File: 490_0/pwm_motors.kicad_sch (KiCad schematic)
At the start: 38 parts, among them J11 S2B-XH-A, J12 S2B-XH-A, J6 S2B-XH-A, J7 S2B-XH-A, J8 S2B-XH-A, Q1 NMOS, Q2 NMOS, Q3 NMOS, Q4 NMOS, Q5 NMOS, U6 PCA9685

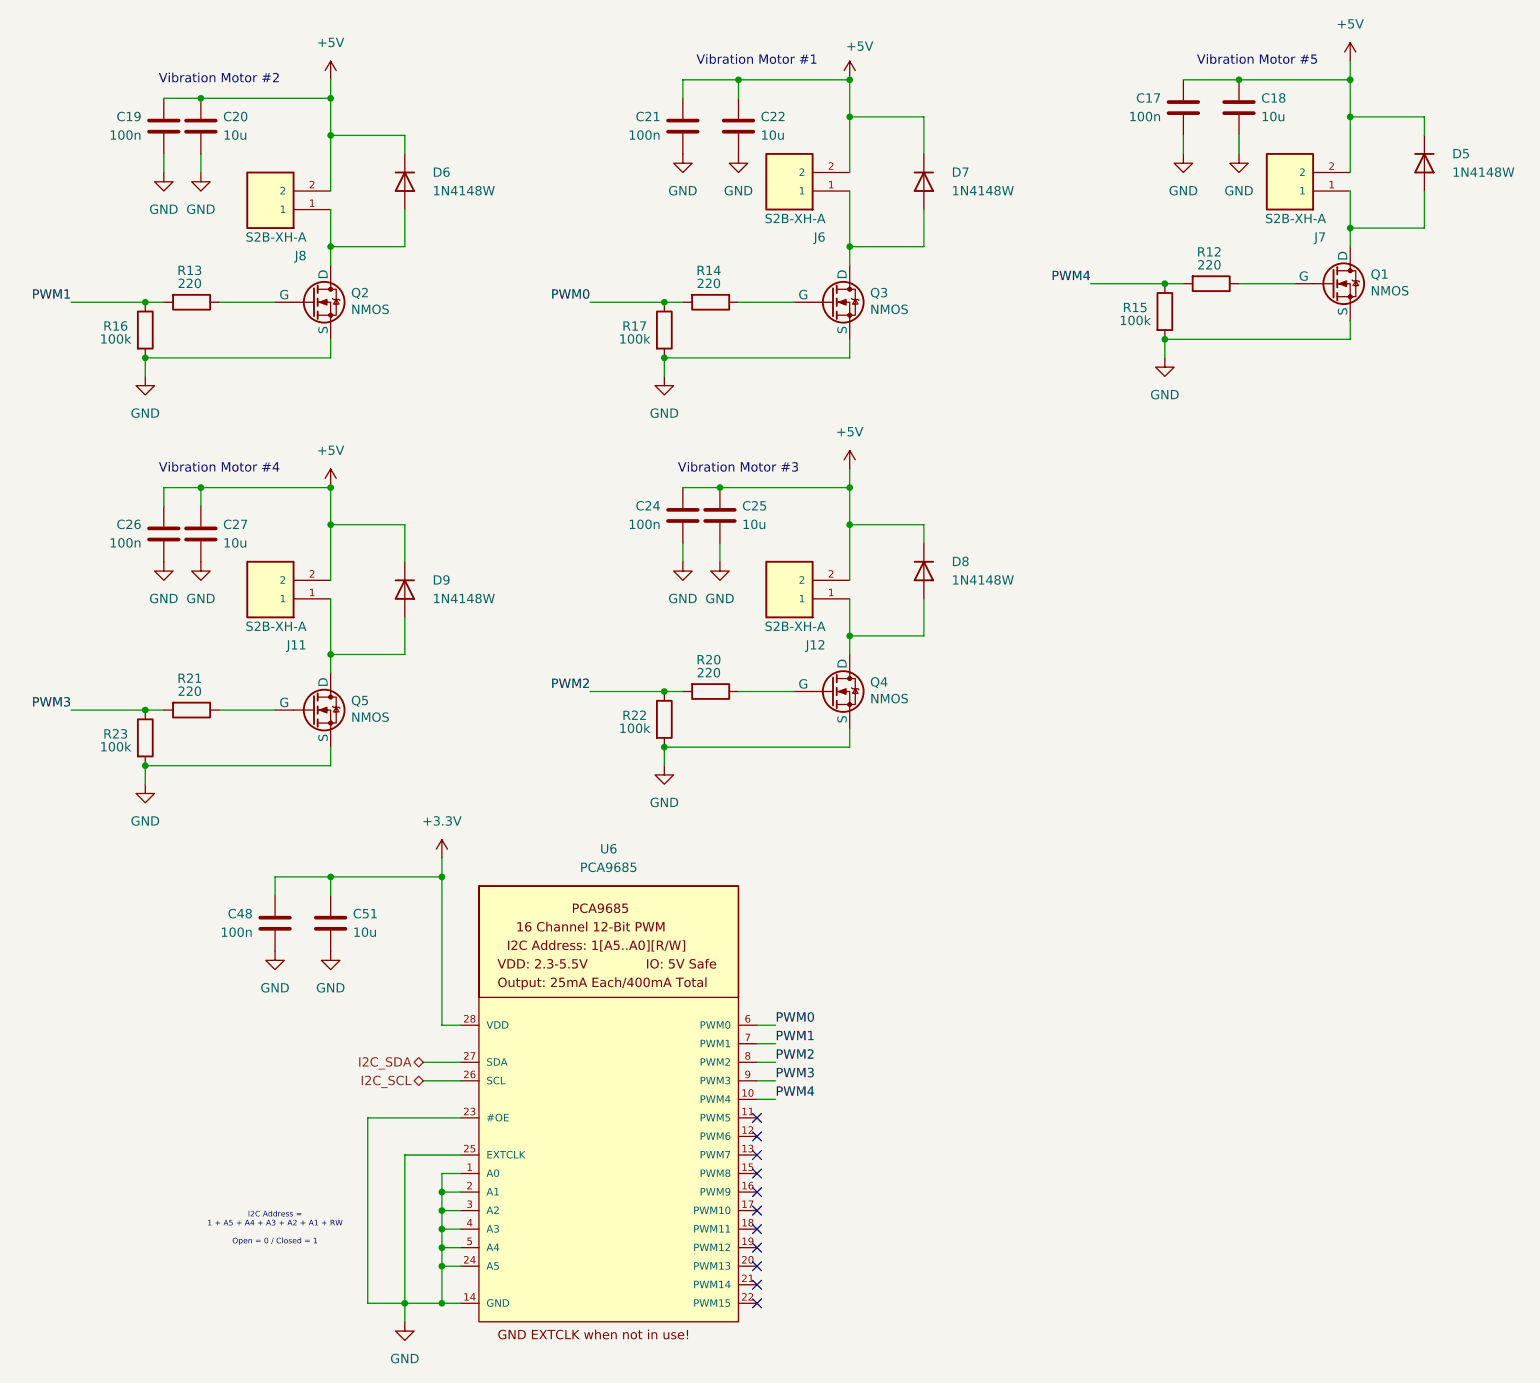
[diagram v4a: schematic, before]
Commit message: Implemented Dmitry comments
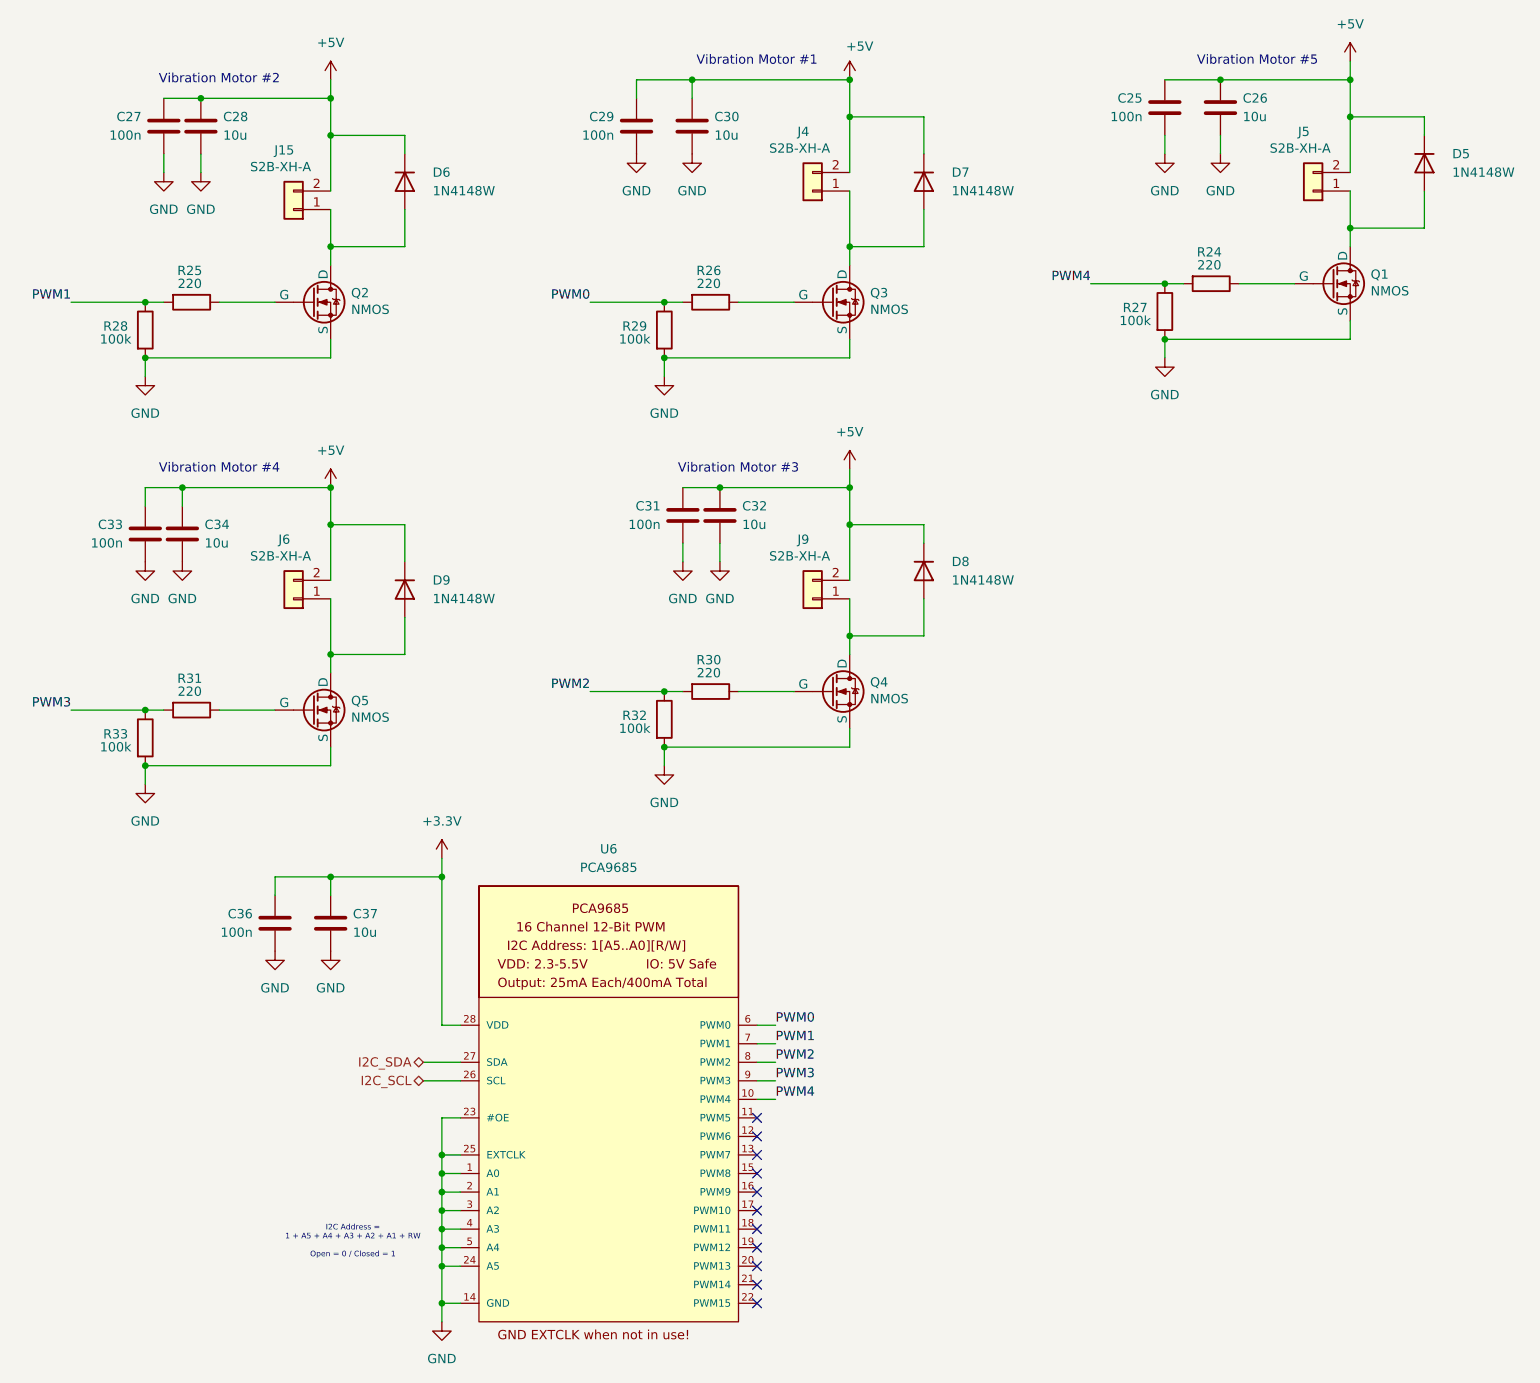
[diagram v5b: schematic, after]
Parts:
- removed J11, J12: S2B-XH-A, 4ms_Connector:Pins_1x08_2.54mm_TH, symbol capstone_parts:S2B-XH-A
- removed J6, J7, J8: S2B-XH-A, S2B-XH-A:JST_S2B-XH-A, symbol capstone_parts:S2B-XH-A
- added J15, J4, J5, J6, J9: S2B-XH-A, S2B-XH-A:JST_S2B-XH-A, symbol PCM_4ms_Connector:Conn_01x02
- renumbered C17 to C25, C18 to C26, C19 to C27, C20 to C28, C21 to C29, C22 to C30, C24 to C31, C25 to C32, C26 to C33, C27 to C34, C48 to C36, C51 to C37, R12 to R24, R13 to R25, R14 to R26, R15 to R27, R16 to R28, R17 to R29, R20 to R30, R21 to R31, R22 to R32, R23 to R33
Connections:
- net +5V: now also J15.2 (Pin_2), J4.2 (Pin_2), J5.2 (Pin_2), J6.2 (Pin_2), J9.2 (Pin_2)
- net at D8.2 (A), Q4.1 (D): now also J9.1 (Pin_1)
- net at D5.2 (A), Q1.1 (D): now also J5.1 (Pin_1)
- net at D6.2 (A), Q2.1 (D): now also J15.1 (Pin_1)
- net at D9.2 (A), Q5.1 (D): now also J6.1 (Pin_1)
- net at D7.2 (A), Q3.1 (D): now also J4.1 (Pin_1)
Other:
- moved on the sheet: C25, C26, C29, C30, C33, C34

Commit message: Final Fixes
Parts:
- J10: renamed from J9; now not fitted; now left out of the parts list
- J4, J5: now not fitted; now left out of the parts list
- J6: renamed from J15; now not fitted; now left out of the parts list
- J9: renamed from J6; now not fitted; now left out of the parts list
- renumbered C25 to C19, C26 to C20, C27 to C21, C28 to C22, C29 to C23, C30 to C24, C31 to C25, C32 to C26, C33 to C27, C34 to C28, C36 to C30, C37 to C31, R24 to R12, R25 to R13, R26 to R14, R27 to R15, R28 to R16, R29 to R17, R30 to R18, R31 to R19, R32 to R20, R33 to R21

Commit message: Implemented Dmitry recommendations
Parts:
- J10, J4, J5, J6, J9: now fitted
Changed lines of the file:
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@@
 		(in_bom no)
 		(on_board yes)
-		(dnp yes)
+		(dnp no)
 		(property "Reference" "J5"
 			(at 201.93 29.972 0)
@@
 		(in_bom no)
 		(on_board yes)
-		(dnp yes)
+		(dnp no)
 		(property "Reference" "J9"
 			(at 62.23 85.852 0)
@@
 		(in_bom no)
 		(on_board yes)
-		(dnp yes)
+		(dnp no)
 		(property "Reference" "J4"
 			(at 133.35 29.972 0)
@@
 		(in_bom no)
 		(on_board yes)
-		(dnp yes)
+		(dnp no)
 		(property "Reference" "J10"
 			(at 133.35 85.852 0)
@@
 		(in_bom no)
 		(on_board yes)
-		(dnp yes)
+		(dnp no)
 		(property "Reference" "J6"
 			(at 62.23 32.512 0)

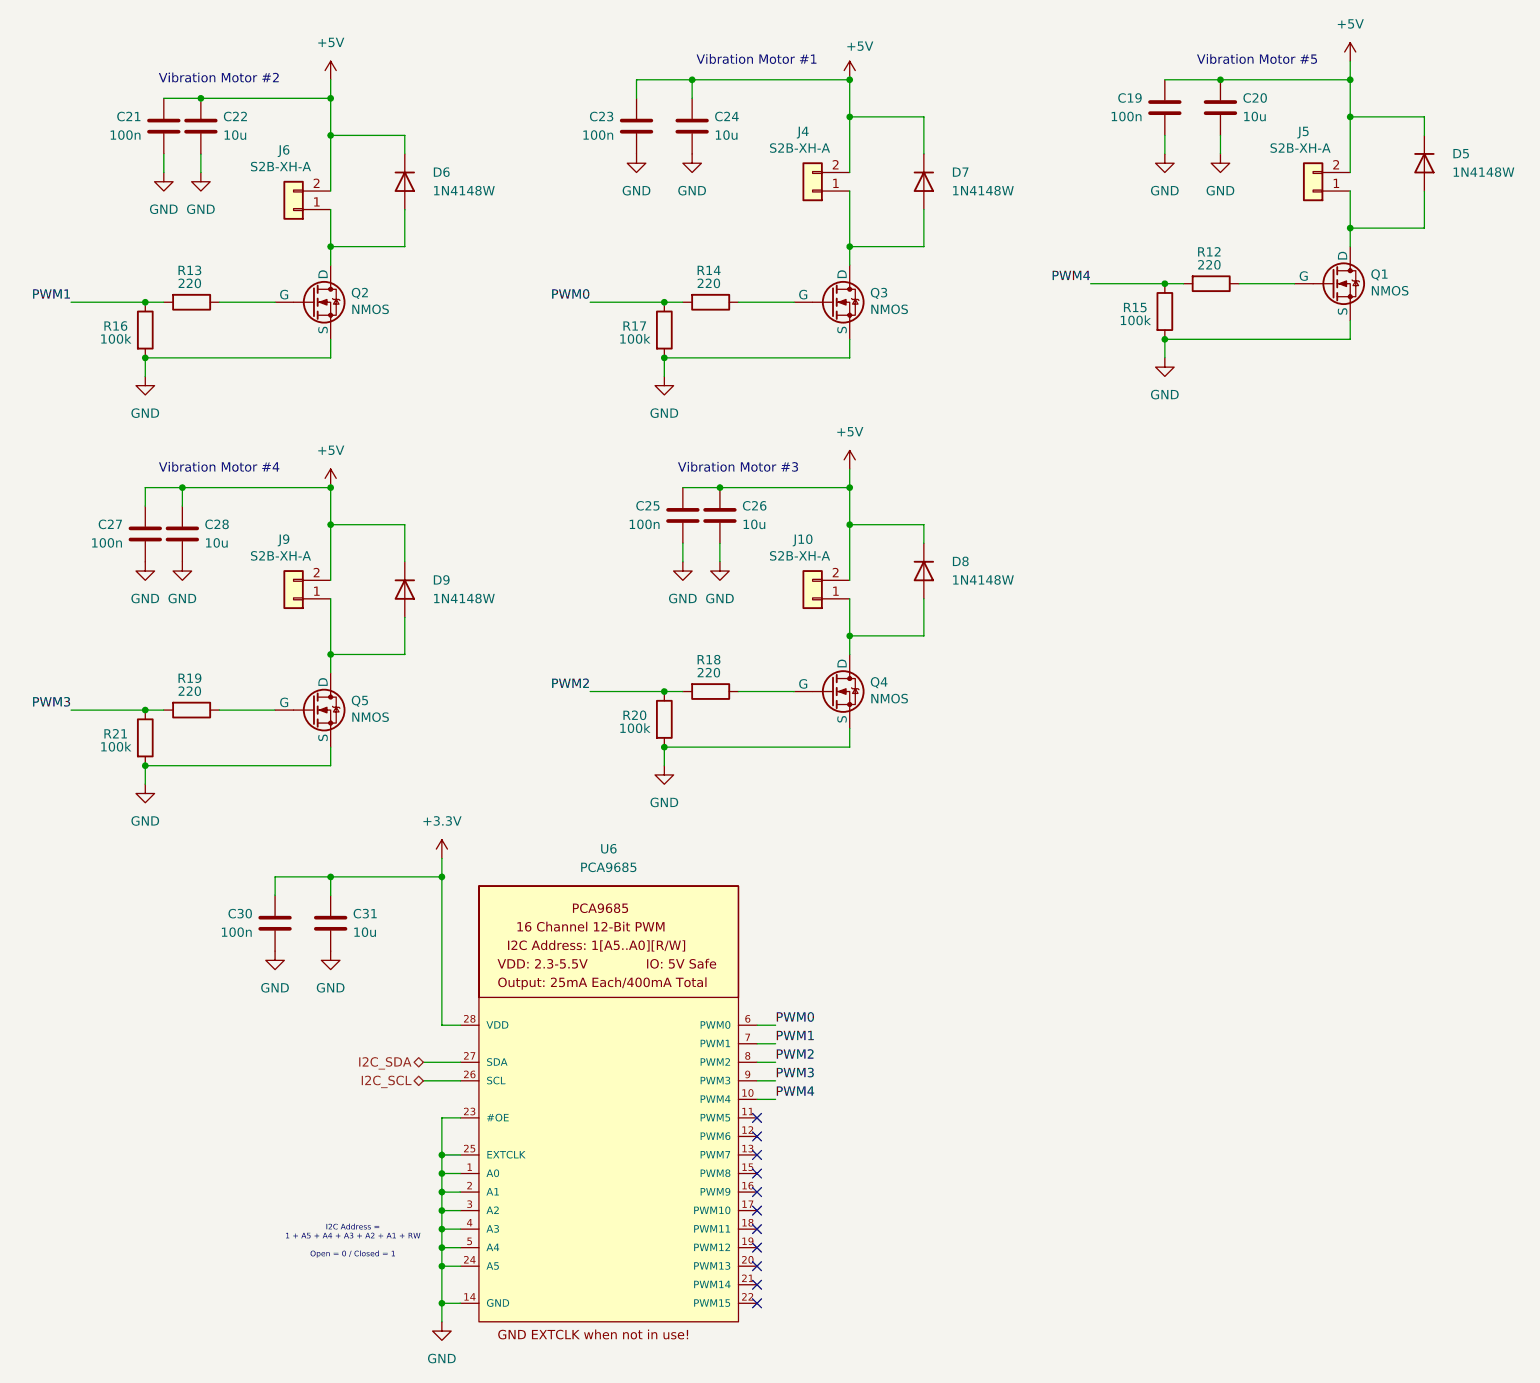
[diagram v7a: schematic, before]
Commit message: FFC to HDMI change
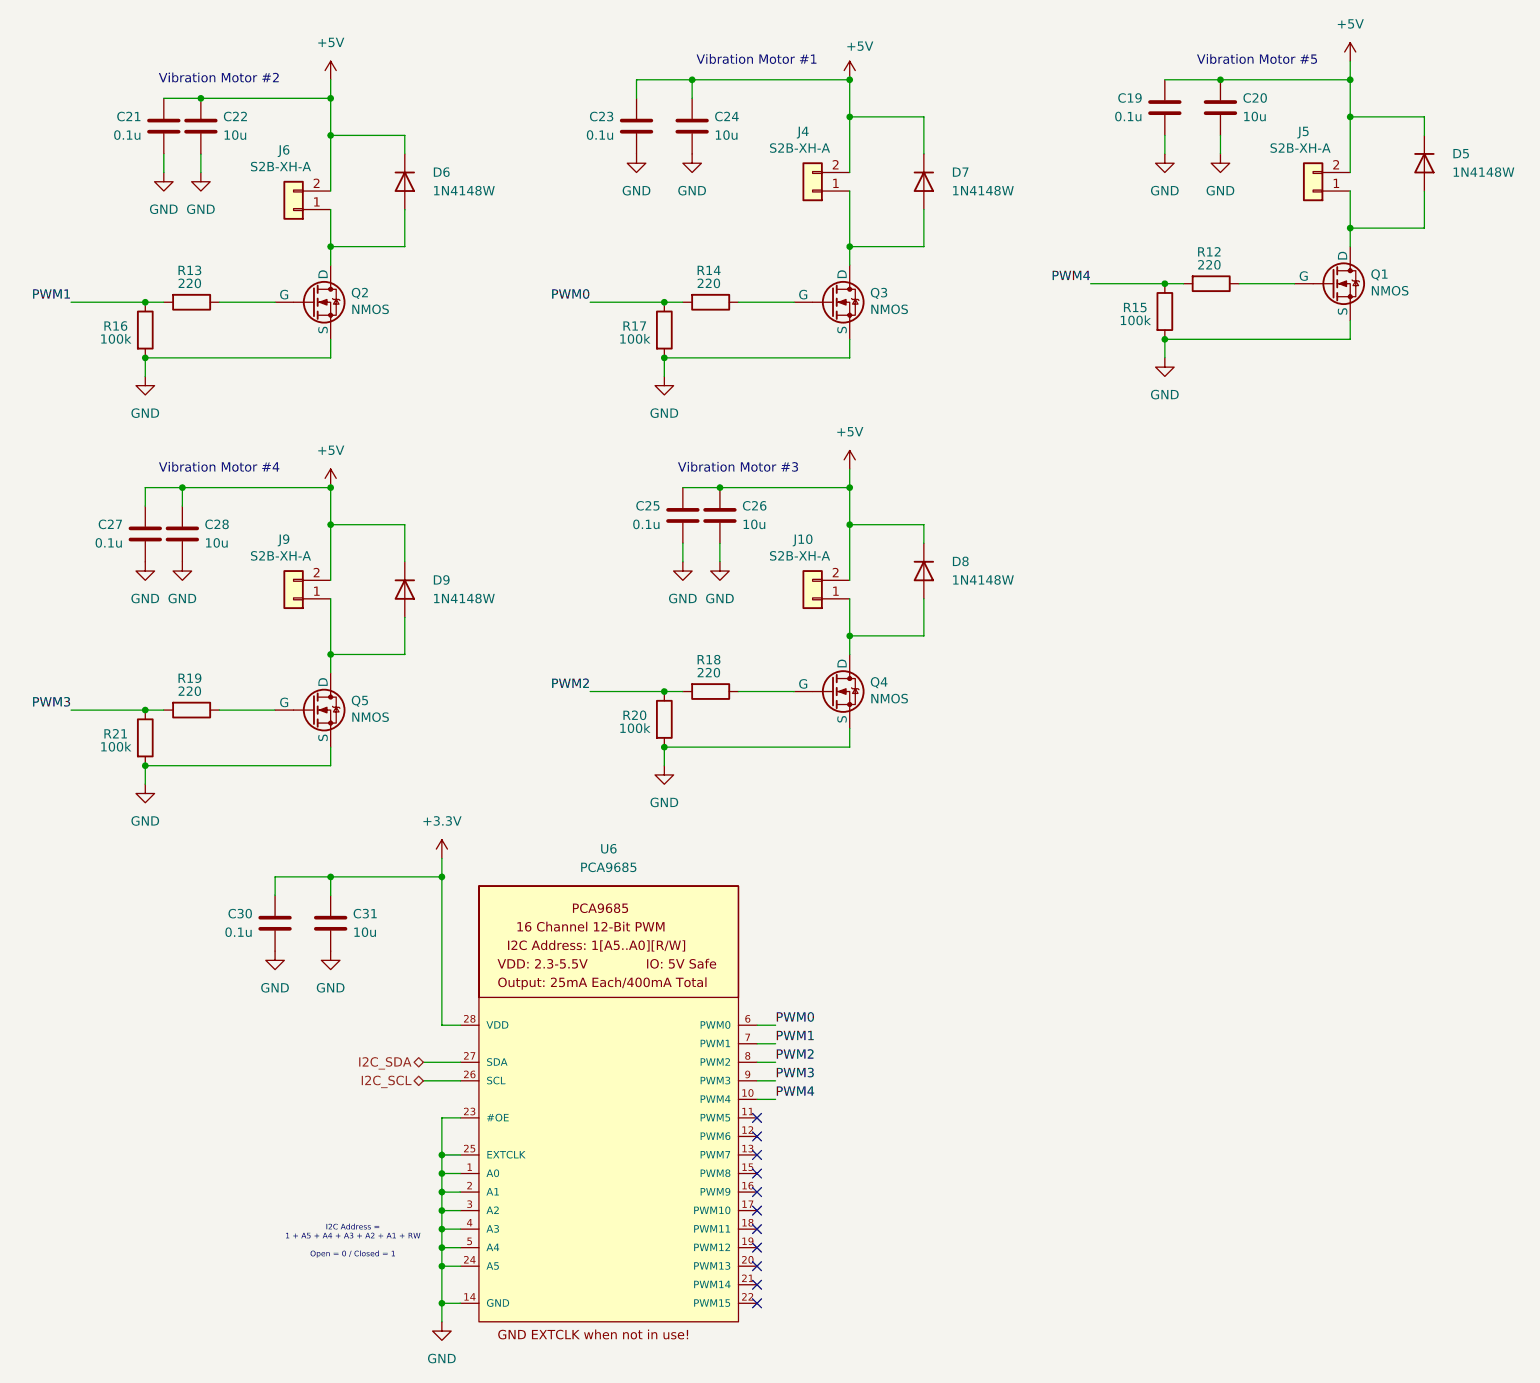
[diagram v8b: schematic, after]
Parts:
- C19, C21, C23, C25, C27, C30: value 100n -> 0.1u
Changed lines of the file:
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@@
 			)
 		)
-		(property "Value" "100n"
+		(property "Value" "0.1u"
 			(at 179.832 27.94 0)
 			(effects
@@
 			)
 		)
-		(property "Value" "100n"
+		(property "Value" "0.1u"
 			(at 40.132 86.36 0)
 			(effects
@@
 			)
 		)
-		(property "Value" "100n"
+		(property "Value" "0.1u"
 			(at 113.792 83.82 0)
 			(effects
@@
 			)
 		)
-		(property "Value" "100n"
+		(property "Value" "0.1u"
 			(at 57.912 139.7 0)
 			(effects
@@
 			)
 		)
-		(property "Value" "100n"
+		(property "Value" "0.1u"
 			(at 107.442 30.48 0)
 			(effects
@@
 			)
 		)
-		(property "Value" "100n"
+		(property "Value" "0.1u"
 			(at 42.672 30.48 0)
 			(effects
